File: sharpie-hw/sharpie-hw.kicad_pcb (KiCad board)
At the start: 2 copper layers, 62.8 x 38.8 mm, 63 parts, among them J2 Conn_01x02_MountingPin, J3 Conn_01x03_MountingPin, J4 Conn_01x08, J5 Conn_01x14, J6 LS021B7DD02, SW1 SW_Push_Cross, SW2 SW_Push_Cross, SW3 SW_Push_Cross, U1 TPS7A2533, U2 TPS7A2501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

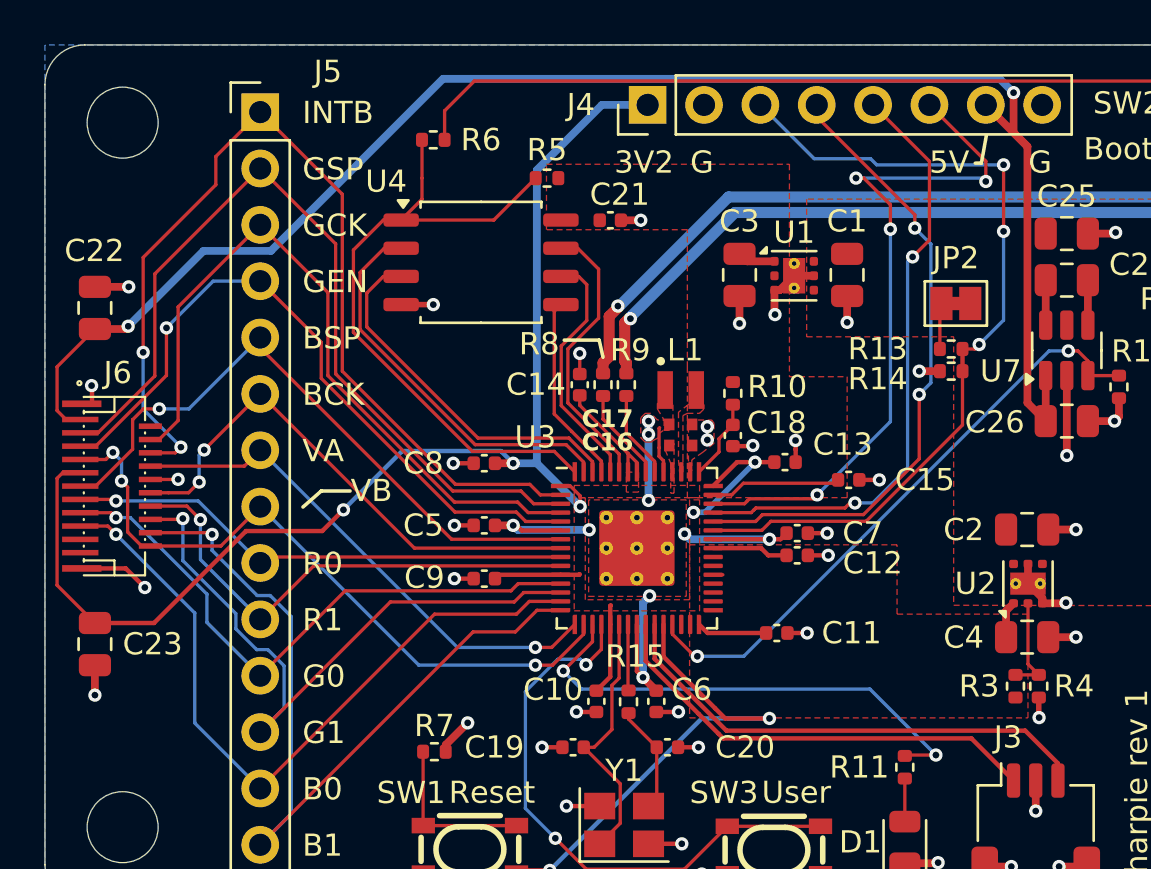
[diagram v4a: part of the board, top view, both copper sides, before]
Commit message: Adjust orientation of necessary parts for JLCPCB assembly.
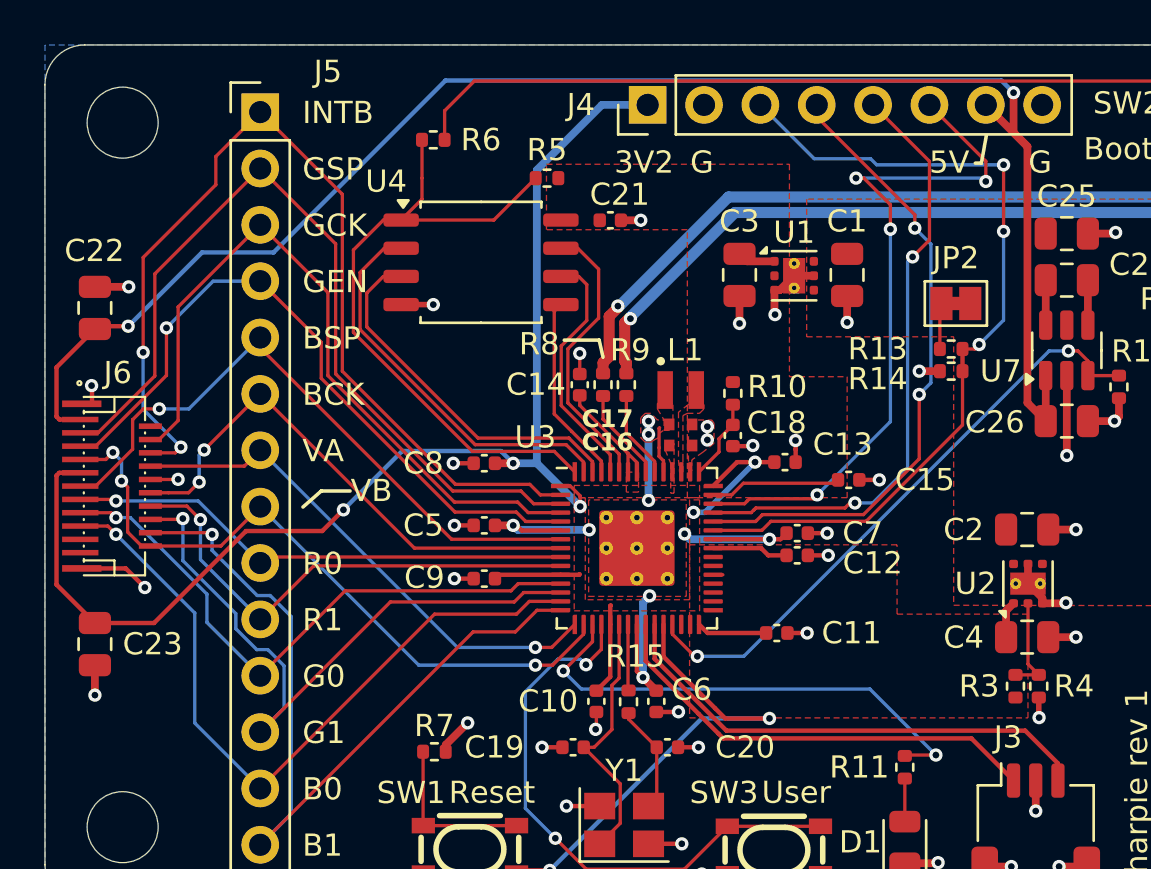
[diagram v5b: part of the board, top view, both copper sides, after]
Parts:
- C22, C23: value 1u -> 1u X7R
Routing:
- net +5V: track 72.5 -> 73.3 mm

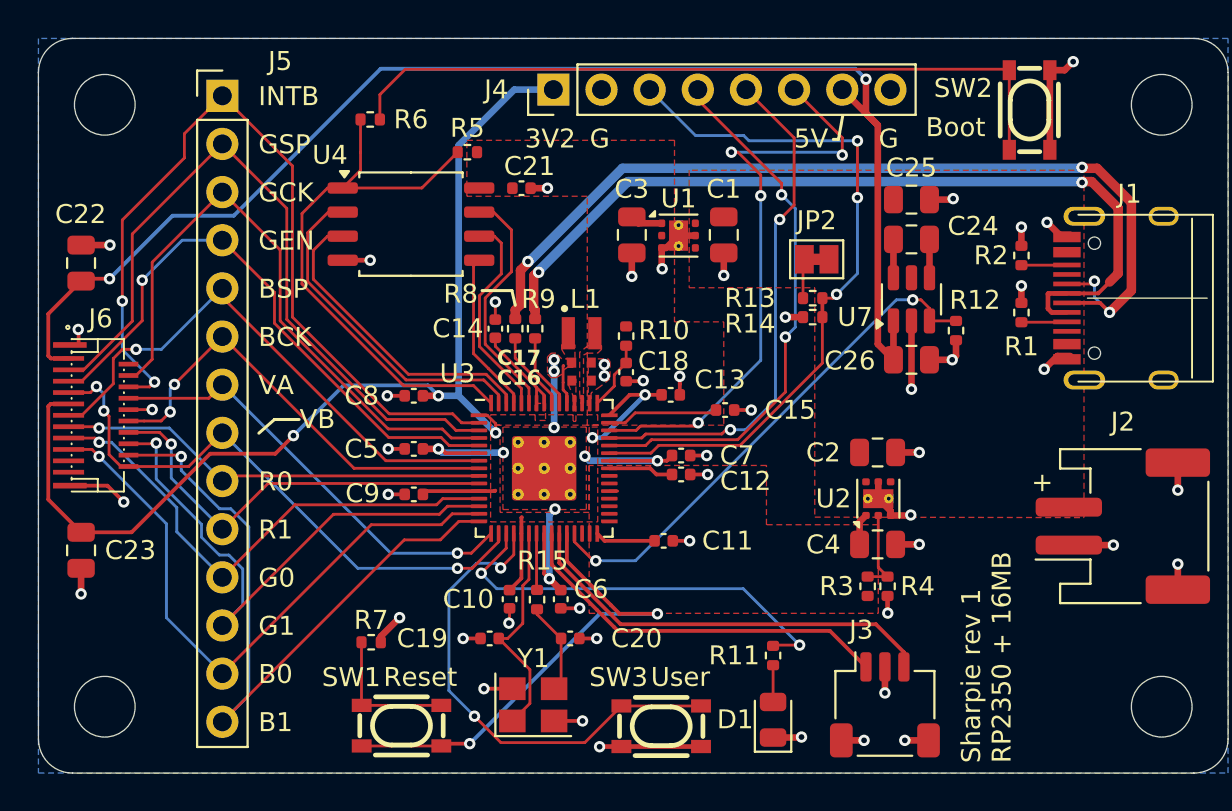
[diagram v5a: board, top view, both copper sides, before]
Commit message: Move to as many JLCPCB basic parts as possible and remove user button.
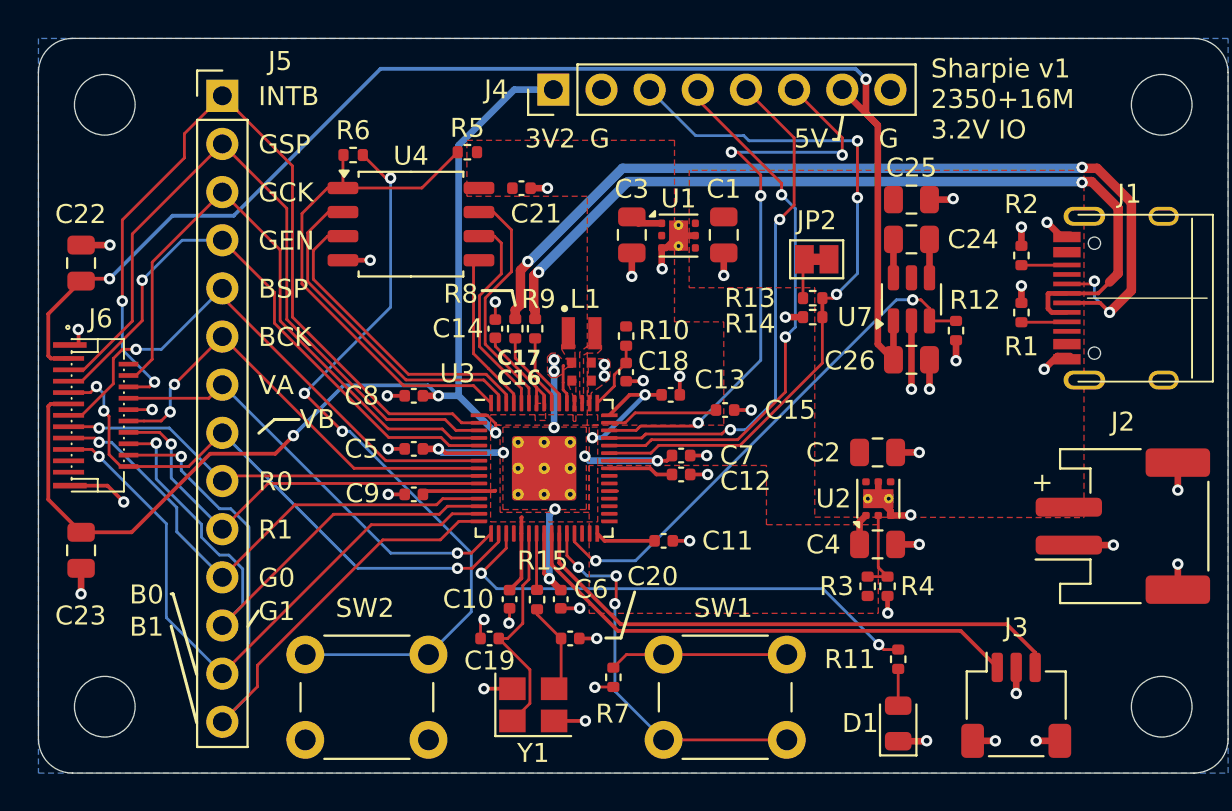
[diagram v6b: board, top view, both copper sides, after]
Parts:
- removed SW3: SW_Push_Cross, Sharpie:KEY-SMD_4P-L4.2-W3.2-P2.20-LS4.6
- SW1, SW2: footprint Sharpie:KEY-SMD_4P-L4.2-W3.2-P2.20-LS4.6 -> Button_Switch_THT:SW_PUSH_6mm
- U4: footprint Package_SO:SOIC-8_5.23x5.23mm_P1.27mm -> Package_SO:SOIC-8_5.3x5.3mm_P1.27mm
- moved SW2 45.9 mm to (213.5, 102.2), turned to 180 degrees
- moved SW1 14.3 mm to (225.9, 97.7)
- moved R7 12.9 mm to (223.2, 98.8), turned to -90 degrees
- moved J3 6.93 mm to (244.5, 100.3)
- moved D1 6.60 mm to (238.2, 101.3)
- moved R11 6.60 mm to (238.2, 97.9)
- moved R6 2.08 mm to (209.5, 71.3)
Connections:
- R6 pad 1: Net-(SW2-2) -> Net-(R6-Pad1)
- SW1 pad 2: Net-(R7-Pad1) -> Net-(U3-RUN)
- SW2 pad 2: GND -> Net-(R6-Pad1)
- U3 pad 19: /MCU/User Btn -> unconnected-(U3-GPIO15-Pad19)
- U3 pad 26: Net-(SW1-2) -> Net-(U3-RUN)
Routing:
- net Net-(R6-Pad1): track 0.00 -> 41.2 mm, vias 0 -> 3
- net Net-(SW2-2): track 39.3 -> 0.00 mm
- net /MCU/User Btn: track 26.0 -> 0.00 mm, vias 2 -> 0
- net Net-(SW1-2): track 25.9 -> 0.00 mm, vias 2 -> 0
- net Net-(U3-RUN): track 0.00 -> 20.5 mm, vias 0 -> 3
- net GND: track 74.2 -> 63.1 mm, vias 50 -> 49
- net /MCU/SWDIO: track 22.8 -> 29.7 mm
- net /MCU/SWCLK: track 20.5 -> 27.4 mm
- net /MCU/User LED: track 22.4 -> 26.4 mm
- net /MCU/QSPI CS: track 29.9 -> 27.6 mm
- net Net-(R7-Pad1): track 7.53 -> 9.44 mm
- net B1: track 37.4 -> 38.0 mm
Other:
- board text added: "Sharpie v1 2350+16M 3.2V IO"
- board text removed: "Boot"
- board text removed: "Reset"
- board text removed: "Sharpie rev 1 RP2350 + 16MB"
- board text removed: "User"

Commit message: Fix two items: battery connector polarity and AP3602 capacitor polarity.
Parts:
- R13: value 27k -> 33k
- moved R12 182.1 mm to (65.0, 35.0), turned to 90 degrees
- moved C26 178.3 mm to (67.4, 33.4), turned to 180 degrees
- moved C1 177.4 mm to (56.6, 33.8)
- moved C12 177.4 mm to (54.3, 46.5)
- moved C16 177.4 mm to (49.1, 41.5)
- moved C17 177.4 mm to (49.1, 40.6)
- moved C18 177.4 mm to (51.4, 41.1)
- moved C7 177.4 mm to (54.3, 45.5)
- moved H2 177.4 mm to (79.7, 27.0)
- moved H4 177.4 mm to (79.7, 58.7)
- moved L1 177.4 mm to (49.1, 39.0)
- moved R10 177.4 mm to (51.4, 39.2)
- moved R13 177.4 mm to (61.3, 37.2)
- moved R14 177.4 mm to (61.3, 38.2)
- moved R5 177.4 mm to (43.0, 29.5)
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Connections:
- C24 pad 1: Net-(U7-C+) -> Net-(U7-C-)
- C24 pad 2: Net-(U7-C-) -> Net-(U7-C+)
- J2 pad 1: GND -> VCC
- J2 pad 2: VCC -> GND
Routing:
- net +5V: track 73.3 -> 67.5 mm
- net GND: track 63.1 -> 58.8 mm, vias 49 -> 47
- net /MCU/User LED: track 26.4 -> 24.3 mm
- net +3.3V: track 12.9 -> 11.2 mm

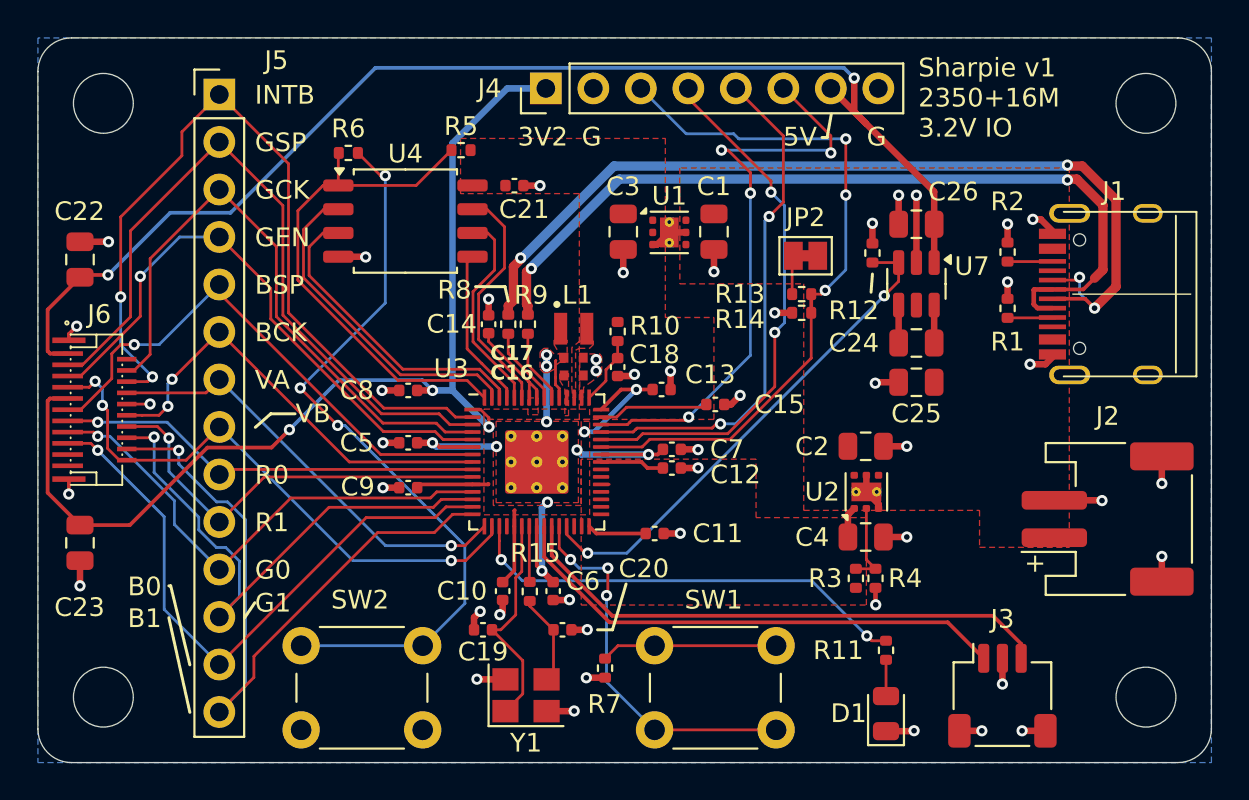
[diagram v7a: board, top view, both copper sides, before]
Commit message: Add vdp_simulator with one tilemap layer rendering, including scroll.
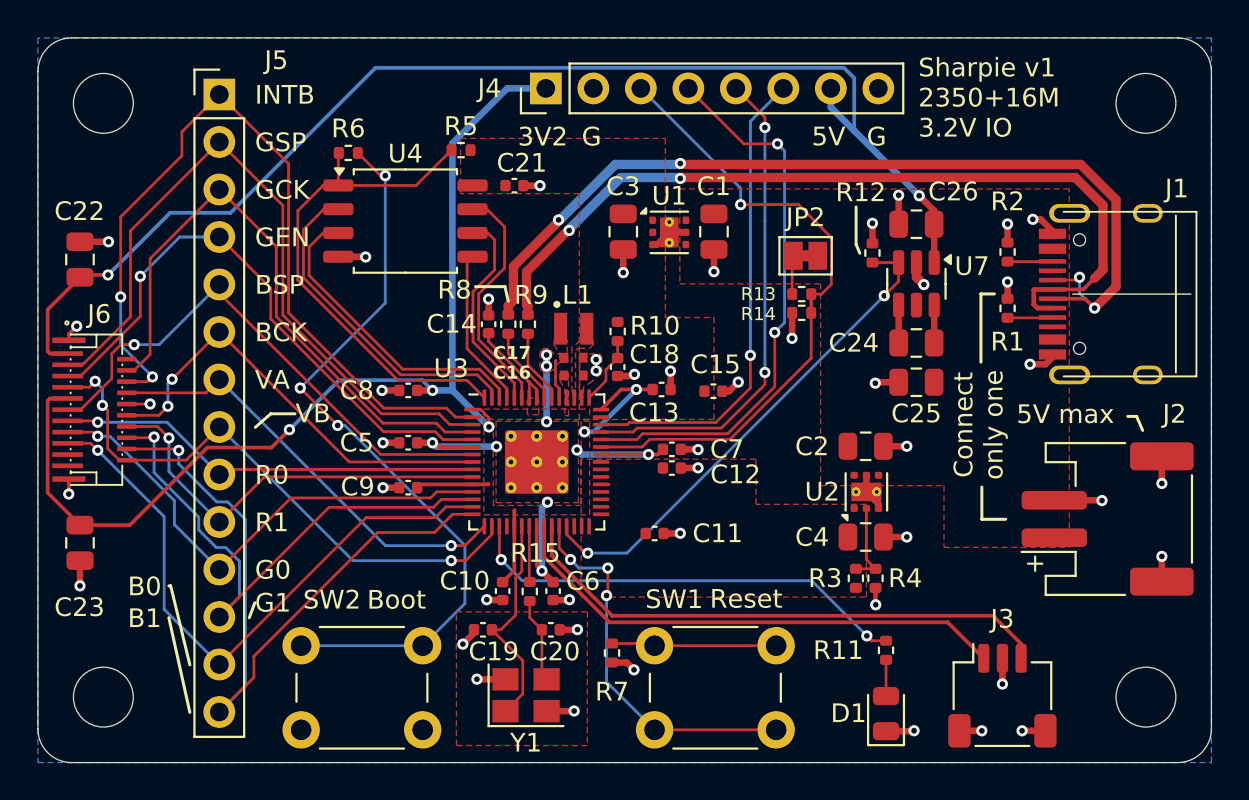
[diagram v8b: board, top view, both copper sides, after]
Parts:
- moved R7 0.89 mm to (51.1, 56.4)
- moved C15 0.72 mm to (56.5, 42.4)
- moved C20 0.62 mm to (47.9, 55.1)
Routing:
- net +3.2V: track 80.0 -> 71.7 mm
- net /MCU/EX_B7: track 31.8 -> 25.5 mm, vias 4 -> 1
- net +3.3V: track 11.2 -> 5.38 mm
- net /MCU/EX_B4: track 38.1 -> 34.4 mm, vias 3 -> 1
- net /MCU/EX_B5: track 28.8 -> 30.3 mm
- net GND: track 58.8 -> 57.3 mm
- net /MCU/EX_B6: track 27.4 -> 26.3 mm
- net Net-(R7-Pad1): track 9.44 -> 8.82 mm
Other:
- board text added: "5V max"
- board text added: "Boot"
- board text added: "Connect only one"
- board text added: "Reset"
